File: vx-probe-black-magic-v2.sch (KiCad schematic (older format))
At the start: 31 parts, among them P1 USB MINI B, U1 stm32f070-qfp48, U2 AT45DB321D-SU, Y1 8 MHz

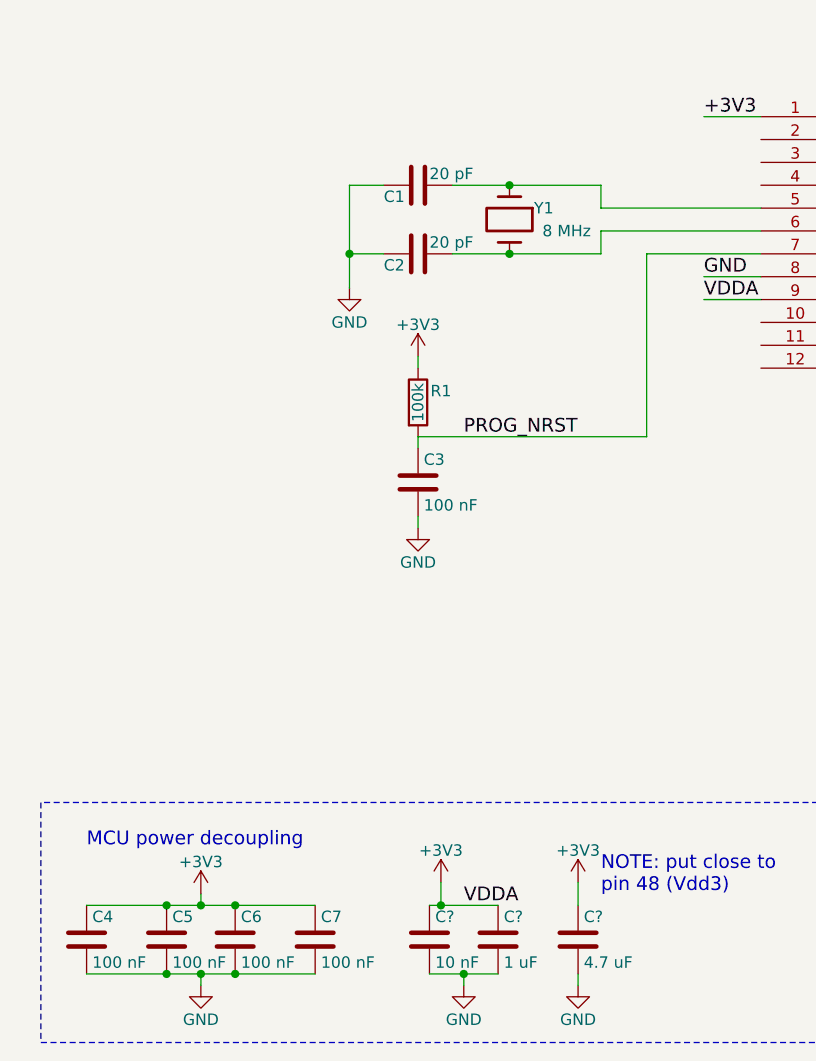
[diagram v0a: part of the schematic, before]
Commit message: made capacitor values more readable
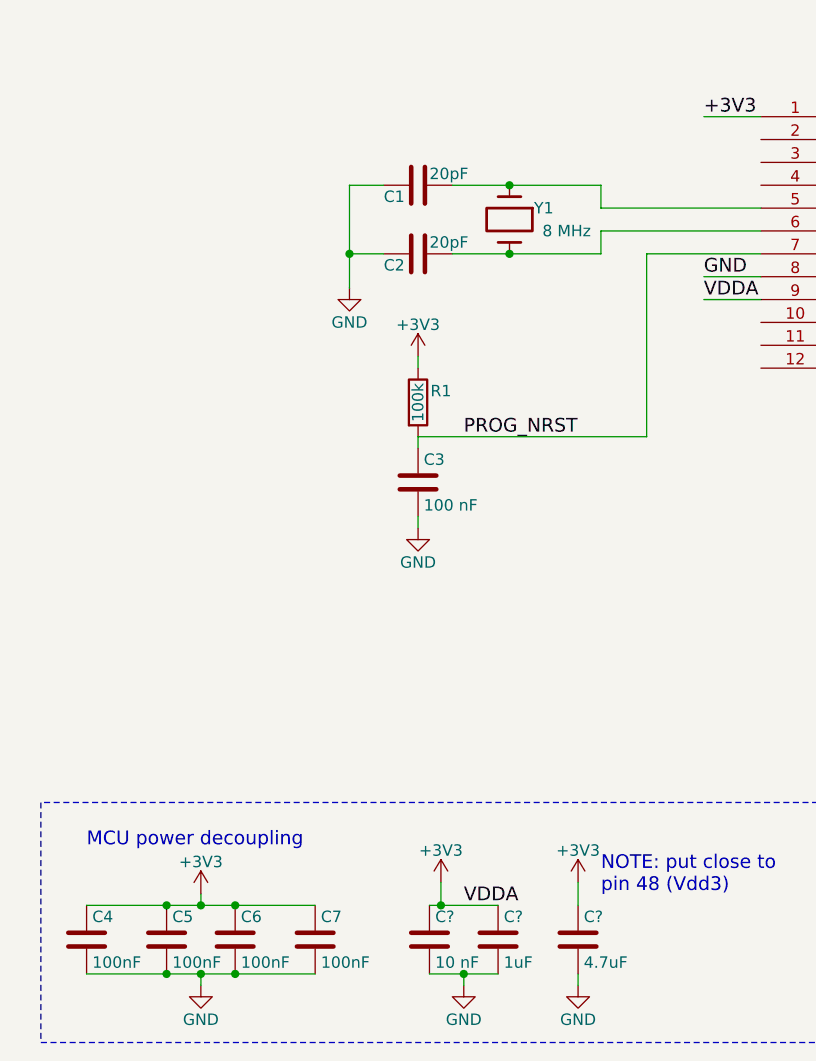
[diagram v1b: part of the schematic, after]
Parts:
- C1, C2: value 20 pF -> 20pF
- C4, C5, C6, C7: value 100 nF -> 100nF
- C?: value 1 uF -> 1uF
- C?: value 4.7 uF -> 4.7uF
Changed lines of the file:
@@
 P 2500 3750
 F 0 "C1" V 2550 3600 50  0000 L CNN
-F 1 "20 pF" V 2450 3800 50  0000 L CNN
+F 1 "20pF" V 2450 3800 50  0000 L CNN
 F 2 "Capacitors_SMD:C_0805" H 2538 3600 50  0001 C CNN
 F 3 "" H 2500 3750 50  0000 C CNN
@@
 P 2500 4050
 F 0 "C2" V 2550 3900 50  0000 L CNN
-F 1 "20 pF" V 2450 4100 50  0000 L CNN
+F 1 "20pF" V 2450 4100 50  0000 L CNN
 F 2 "Capacitors_SMD:C_0805" H 2538 3900 50  0001 C CNN
 F 3 "" H 2500 4050 50  0000 C CNN
@@
 P 1050 7050
 F 0 "C4" H 1075 7150 50  0000 L CNN
-F 1 "100 nF" H 1075 6950 50  0000 L CNN
+F 1 "100nF" H 1075 6950 50  0000 L CNN
 F 2 "Capacitors_SMD:C_0805" H 1088 6900 50  0001 C CNN
 F 3 "" H 1050 7050 50  0000 C CNN
@@
 P 1400 7050
 F 0 "C5" H 1425 7150 50  0000 L CNN
-F 1 "100 nF" H 1425 6950 50  0000 L CNN
+F 1 "100nF" H 1425 6950 50  0000 L CNN
 F 2 "Capacitors_SMD:C_0805" H 1438 6900 50  0001 C CNN
 F 3 "" H 1400 7050 50  0000 C CNN
@@
 P 1700 7050
 F 0 "C6" H 1725 7150 50  0000 L CNN
-F 1 "100 nF" H 1725 6950 50  0000 L CNN
+F 1 "100nF" H 1725 6950 50  0000 L CNN
 F 2 "Capacitors_SMD:C_0805" H 1738 6900 50  0001 C CNN
 F 3 "" H 1700 7050 50  0000 C CNN
@@
 P 2050 7050
 F 0 "C7" H 2075 7150 50  0000 L CNN
-F 1 "100 nF" H 2075 6950 50  0000 L CNN
+F 1 "100nF" H 2075 6950 50  0000 L CNN
 F 2 "Capacitors_SMD:C_0805" H 2088 6900 50  0001 C CNN
 F 3 "" H 2050 7050 50  0000 C CNN
@@
 P 2850 7050
 F 0 "C?" H 2875 7150 50  0000 L CNN
-F 1 "1 uF" H 2875 6950 50  0000 L CNN
+F 1 "1uF" H 2875 6950 50  0000 L CNN
 F 2 "" H 2888 6900 50  0000 C CNN
 F 3 "" H 2850 7050 50  0000 C CNN
@@
 P 3200 7050
 F 0 "C?" H 3225 7150 50  0000 L CNN
-F 1 "4.7 uF" H 3225 6950 50  0000 L CNN
+F 1 "4.7uF" H 3225 6950 50  0000 L CNN
 F 2 "" H 3238 6900 50  0000 C CNN
 F 3 "" H 3200 7050 50  0000 C CNN

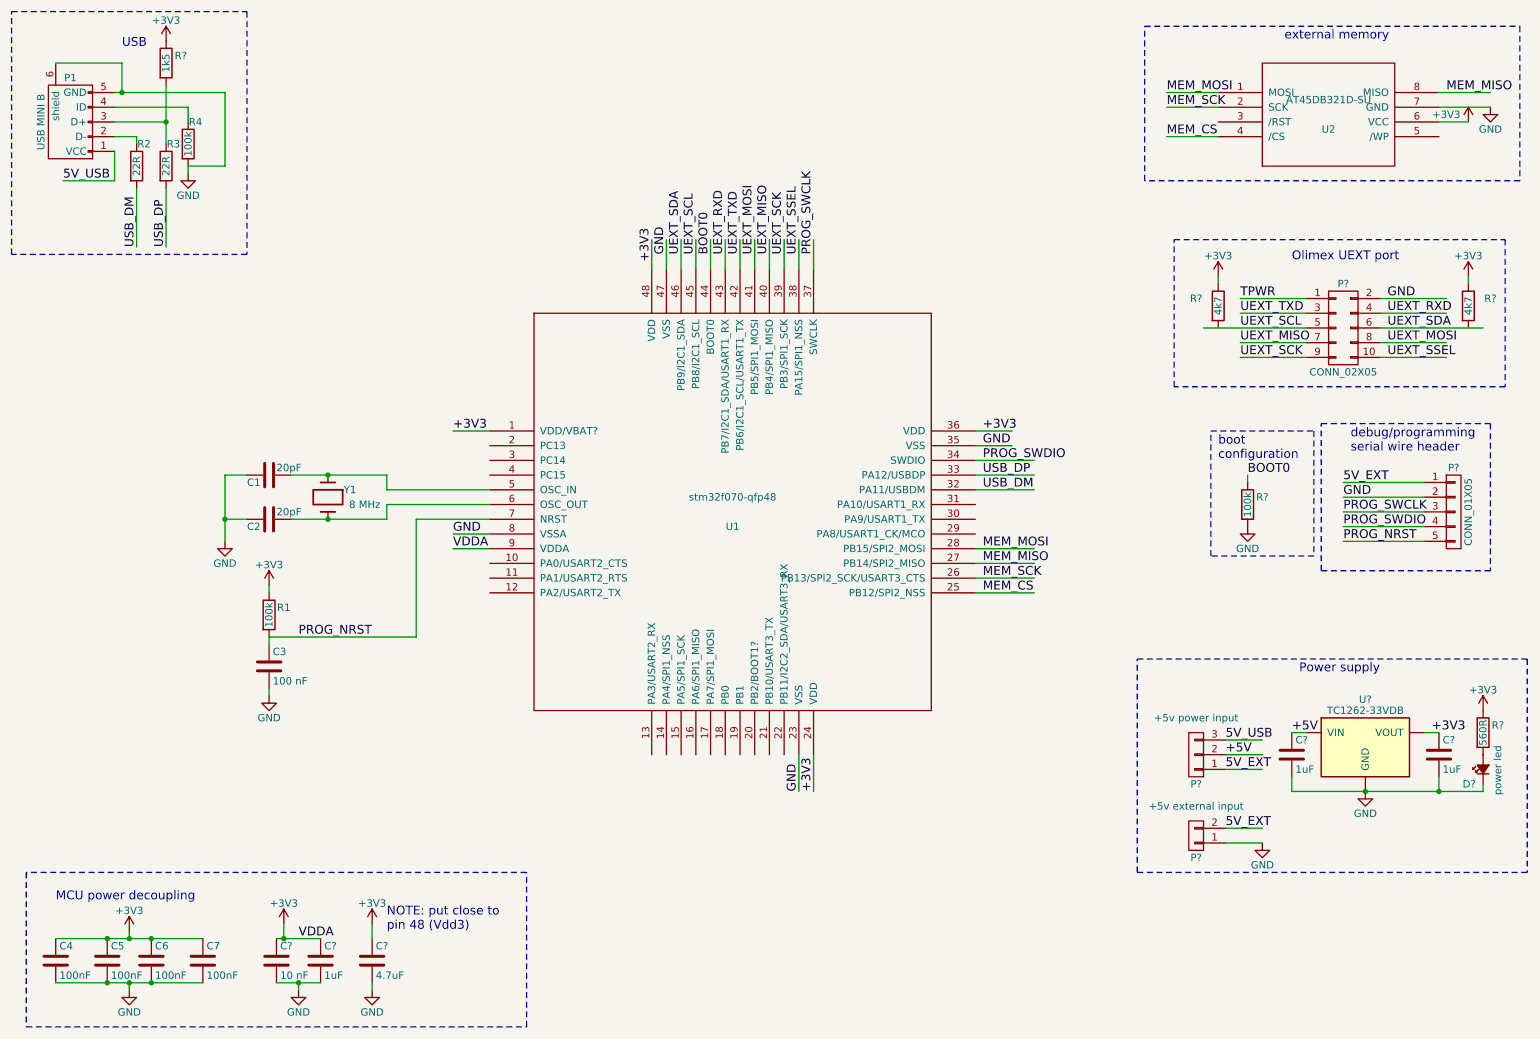
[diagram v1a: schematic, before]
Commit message: updated components' annotations and footprints
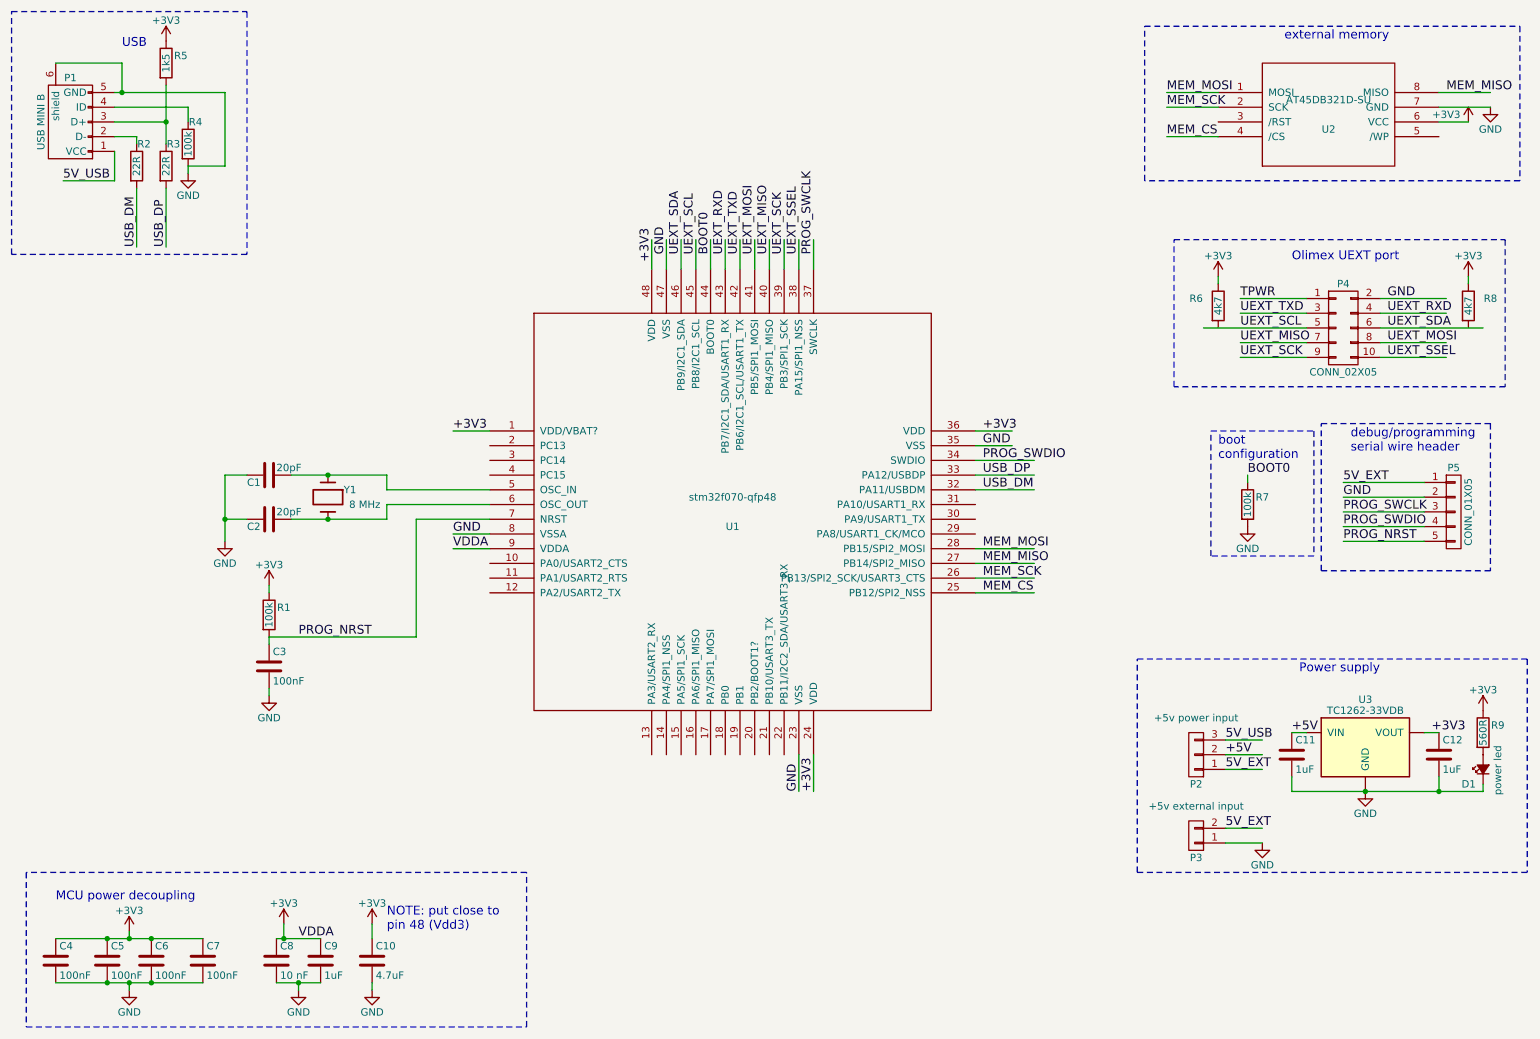
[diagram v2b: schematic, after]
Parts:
- C10, C11, C12, C8, C9: renamed from C?; footprint (none) -> Capacitors_SMD:C_0805
- C3: value 100 nF -> 100nF
- D1: renamed from D?; footprint (none) -> LEDs:LED_0805
- P2: renamed from P?; footprint (none) -> Pin_Headers:Pin_Header_Straight_1x03
- P3: renamed from P?; footprint (none) -> Pin_Headers:Pin_Header_Straight_1x02
- P4: renamed from P?; footprint (none) -> Pin_Headers:Pin_Header_Straight_2x05
- P5: renamed from P?; footprint (none) -> Pin_Headers:Pin_Header_Straight_1x05
- R5, R6, R7, R8, R9: renamed from R?; footprint (none) -> Resistors_SMD:R_0805
- U3: renamed from U?; footprint SOT-223 -> TO_SOT_Packages_SMD:SOT-223
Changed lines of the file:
@@
 P 2500 5050
 F 0 "C3" H 2525 5150 50  0000 L CNN
-F 1 "100 nF" H 2525 4950 50  0000 L CNN
+F 1 "100nF" H 2525 4950 50  0000 L CNN
 F 2 "Capacitors_SMD:C_0805" H 2538 4900 50  0001 C CNN
 F 3 "" H 2500 5050 50  0000 C CNN
@@
 MEM_MISO
 $Comp
-L +3V3 #PWR?
+L +3V3 #PWR07
 U 1 1 57D8566A
 P 10650 1350
-F 0 "#PWR?" H 10650 1200 50  0001 C CNN
+F 0 "#PWR07" H 10650 1200 50  0001 C CNN
 F 1 "+3V3" H 10500 1400 50  0000 C CNN
 F 2 "" H 10650 1350 50  0000 C CNN
@@
 $EndComp
 $Comp
-L GND #PWR?
+L GND #PWR08
 U 1 1 57D856D3
 P 10800 1250
-F 0 "#PWR?" H 10800 1000 50  0001 C CNN
+F 0 "#PWR08" H 10800 1000 50  0001 C CNN
 F 1 "GND" H 10800 1100 50  0000 C CNN
 F 2 "" H 10800 1250 50  0000 C CNN
@@
 external memory
 $Comp
-L CONN_02X05 P?
+L CONN_02X05 P4
 U 1 1 57D86033
 P 9800 2750
-F 0 "P?" H 9800 3050 50  0000 C CNN
+F 0 "P4" H 9800 3050 50  0000 C CNN
 F 1 "CONN_02X05" H 9800 2450 50  0000 C CNN
-F 2 "" H 9800 1550 50  0000 C CNN
+F 2 "Pin_Headers:Pin_Header_Straight_2x05" H 9800 1550 50  0001 C CNN
 F 3 "" H 9800 1550 50  0000 C CNN
 	1    9800 2750
@@
 UEXT_SSEL
 $Comp
-L R R?
+L R R6
 U 1 1 57D8663E
 P 8950 2600
-F 0 "R?" H 8800 2650 50  0000 C CNN
+F 0 "R6" H 8800 2650 50  0000 C CNN
 F 1 "4k7" V 8950 2600 50  0000 C CNN
-F 2 "" V 8880 2600 50  0000 C CNN
+F 2 "Resistors_SMD:R_0805" V 8880 2600 50  0001 C CNN
 F 3 "" H 8950 2600 50  0000 C CNN
 	1    8950 2600
@@
 $EndComp
 $Comp
-L +3V3 #PWR?
+L +3V3 #PWR09
 U 1 1 57D86D6F
 P 8950 2400
-F 0 "#PWR?" H 8950 2250 50  0001 C CNN
+F 0 "#PWR09" H 8950 2250 50  0001 C CNN
 F 1 "+3V3" H 8950 2540 50  0000 C CNN
 F 2 "" H 8950 2400 50  0000 C CNN
@@
 $EndComp
 $Comp
-L R R?
+L R R8
 U 1 1 57D86DD6
 P 10650 2600
-F 0 "R?" H 10800 2650 50  0000 C CNN
+F 0 "R8" H 10800 2650 50  0000 C CNN
 F 1 "4k7" V 10650 2600 50  0000 C CNN
-F 2 "" V 10580 2600 50  0000 C CNN
+F 2 "Resistors_SMD:R_0805" V 10580 2600 50  0001 C CNN
 F 3 "" H 10650 2600 50  0000 C CNN
 	1    10650 2600
@@
 $EndComp
 $Comp
-L +3V3 #PWR?
+L +3V3 #PWR010
 U 1 1 57D86DDD
 P 10650 2400
-F 0 "#PWR?" H 10650 2250 50  0001 C CNN
+F 0 "#PWR010" H 10650 2250 50  0001 C CNN
 F 1 "+3V3" H 10650 2540 50  0000 C CNN
 F 2 "" H 10650 2400 50  0000 C CNN
@@
 VDDA
 $Comp
-L C C?
+L C C8
 U 1 1 57D889A2
 P 2550 7050
-F 0 "C?" H 2575 7150 50  0000 L CNN
+F 0 "C8" H 2575 7150 50  0000 L CNN
 F 1 "10 nF" H 2575 6950 50  0000 L CNN
-F 2 "" H 2588 6900 50  0000 C CNN
+F 2 "Capacitors_SMD:C_0805" H 2588 6900 50  0001 C CNN
 F 3 "" H 2550 7050 50  0000 C CNN
 	1    2550 7050
@@
 $EndComp
 $Comp
-L C C?
+L C C9
 U 1 1 57D88A0C
 P 2850 7050
-F 0 "C?" H 2875 7150 50  0000 L CNN
+F 0 "C9" H 2875 7150 50  0000 L CNN
 F 1 "1uF" H 2875 6950 50  0000 L CNN
-F 2 "" H 2888 6900 50  0000 C CNN
+F 2 "Capacitors_SMD:C_0805" H 2888 6900 50  0001 C CNN
 F 3 "" H 2850 7050 50  0000 C CNN
 	1    2850 7050
@@
 $EndComp
 $Comp
-L GND #PWR?
+L GND #PWR011
 U 1 1 57D88BF4
 P 2700 7250
-F 0 "#PWR?" H 2700 7000 50  0001 C CNN
+F 0 "#PWR011" H 2700 7000 50  0001 C CNN
 F 1 "GND" H 2700 7100 50  0000 C CNN
 F 2 "" H 2700 7250 50  0000 C CNN
@@
 $EndComp
 $Comp
-L +3V3 #PWR?
+L +3V3 #PWR012
 U 1 1 57D88CB2
 P 2600 6800
-F 0 "#PWR?" H 2600 6650 50  0001 C CNN
+F 0 "#PWR012" H 2600 6650 50  0001 C CNN
 F 1 "+3V3" H 2600 6940 50  0000 C CNN
 F 2 "" H 2600 6800 50  0000 C CNN
@@
 VDDA
 $Comp
-L C C?
+L C C10
 U 1 1 57D88F0B
 P 3200 7050
-F 0 "C?" H 3225 7150 50  0000 L CNN
+F 0 "C10" H 3225 7150 50  0000 L CNN
 F 1 "4.7uF" H 3225 6950 50  0000 L CNN
-F 2 "" H 3238 6900 50  0000 C CNN
+F 2 "Capacitors_SMD:C_0805" H 3238 6900 50  0001 C CNN
 F 3 "" H 3200 7050 50  0000 C CNN
 	1    3200 7050
@@
 $EndComp
 $Comp
-L GND #PWR?
+L GND #PWR013
 U 1 1 57D88FD9
 P 3200 7250
-F 0 "#PWR?" H 3200 7000 50  0001 C CNN
+F 0 "#PWR013" H 3200 7000 50  0001 C CNN
 F 1 "GND" H 3200 7100 50  0000 C CNN
 F 2 "" H 3200 7250 50  0000 C CNN
@@
 $EndComp
 $Comp
-L +3V3 #PWR?
+L +3V3 #PWR014
 U 1 1 57D890F4
 P 3200 6800
-F 0 "#PWR?" H 3200 6650 50  0001 C CNN
+F 0 "#PWR014" H 3200 6650 50  0001 C CNN
 F 1 "+3V3" H 3200 6940 50  0000 C CNN
 F 2 "" H 3200 6800 50  0000 C CNN
@@
 NOTE: put close to\npin 48 (Vdd3)
 $Comp
-L R R?
+L R R5
 U 1 1 57D89DD6
 P 1800 950
-F 0 "R?" H 1900 1000 50  0000 C CNN
+F 0 "R5" H 1900 1000 50  0000 C CNN
 F 1 "1k5" V 1800 950 50  0000 C CNN
-F 2 "" V 1730 950 50  0000 C CNN
+F 2 "Resistors_SMD:R_0805" V 1730 950 50  0001 C CNN
 F 3 "" H 1800 950 50  0000 C CNN
 	1    1800 950
@@
 $EndComp
 $Comp
-L +3V3 #PWR?
+L +3V3 #PWR015
 U 1 1 57D89E25
 P 1800 800
-F 0 "#PWR?" H 1800 650 50  0001 C CNN
+F 0 "#PWR015" H 1800 650 50  0001 C CNN
 F 1 "+3V3" H 1800 940 50  0000 C CNN
 F 2 "" H 1800 800 50  0000 C CNN
@@
 PROG_SWCLK
 $Comp
-L CONN_01X05 P?
+L CONN_01X05 P5
 U 1 1 57D8BC7C
 P 10550 4000
-F 0 "P?" H 10550 4300 50  0000 C CNN
+F 0 "P5" H 10550 4300 50  0000 C CNN
 F 1 "CONN_01X05" V 10650 4000 50  0000 C CNN
-F 2 "" H 10550 4000 50  0000 C CNN
+F 2 "Pin_Headers:Pin_Header_Straight_1x05" H 10550 4000 50  0001 C CNN
 F 3 "" H 10550 4000 50  0000 C CNN
 	1    10550 4000
@@
 boot\nconfiguration
 $Comp
-L R R?
+L R R7
 U 1 1 57D8D839
 P 9150 3950
-F 0 "R?" H 9250 4000 50  0000 C CNN
+F 0 "R7" H 9250 4000 50  0000 C CNN
 F 1 "100k" V 9150 3950 50  0000 C CNN
-F 2 "" V 9080 3950 50  0000 C CNN
+F 2 "Resistors_SMD:R_0805" V 9080 3950 50  0001 C CNN
 F 3 "" H 9150 3950 50  0000 C CNN
 	1    9150 3950
@@
 $EndComp
 $Comp
-L GND #PWR?
+L GND #PWR016
 U 1 1 57D8DA47
 P 9150 4100
-F 0 "#PWR?" H 9150 3850 50  0001 C CNN
+F 0 "#PWR016" H 9150 3850 50  0001 C CNN
 F 1 "GND" H 9150 3950 50  0000 C CNN
 F 2 "" H 9150 4100 50  0000 C CNN
@@
 BOOT0
 $Comp
-L TC1262-33VDB U?
+L TC1262-33VDB U3
 U 1 1 57D8E183
 P 9950 5600
-F 0 "U?" H 9950 5925 50  0000 C CNN
+F 0 "U3" H 9950 5925 50  0000 C CNN
 F 1 "TC1262-33VDB" H 9950 5850 50  0000 C CNN
-F 2 "SOT-223" H 10000 5350 50  0001 L CIN
+F 2 "TO_SOT_Packages_SMD:SOT-223" H 10000 5350 50  0001 L CIN
 F 3 "" H 9950 5400 50  0001 C CNN
 	1    9950 5600
@@
 $EndComp
 $Comp
-L C C?
+L C C12
 U 1 1 57D8E350
 P 10450 5650
-F 0 "C?" H 10475 5750 50  0000 L CNN
+F 0 "C12" H 10475 5750 50  0000 L CNN
 F 1 "1uF" H 10475 5550 50  0000 L CNN
-F 2 "" H 10488 5500 50  0000 C CNN
+F 2 "Capacitors_SMD:C_0805" H 10488 5500 50  0001 C CNN
 F 3 "" H 10450 5650 50  0000 C CNN
 	1    10450 5650
@@
 $EndComp
 $Comp
-L C C?
+L C C11
 U 1 1 57D8E408
 P 9450 5650
-F 0 "C?" H 9475 5750 50  0000 L CNN
+F 0 "C11" H 9475 5750 50  0000 L CNN
 F 1 "1uF" H 9475 5550 50  0000 L CNN
-F 2 "" H 9488 5500 50  0000 C CNN
+F 2 "Capacitors_SMD:C_0805" H 9488 5500 50  0001 C CNN
 F 3 "" H 9450 5650 50  0000 C CNN
 	1    9450 5650
@@
 +5V
 $Comp
-L GND #PWR?
+L GND #PWR017
 U 1 1 57D8EA04
 P 9950 5900
-F 0 "#PWR?" H 9950 5650 50  0001 C CNN
+F 0 "#PWR017" H 9950 5650 50  0001 C CNN
 F 1 "GND" H 9950 5750 50  0000 C CNN
 F 2 "" H 9950 5900 50  0000 C CNN
@@
 $EndComp
 $Comp
-L R R?
+L R R9
 U 1 1 57D8EC19
 P 10750 5500
-F 0 "R?" H 10850 5550 50  0000 C CNN
+F 0 "R9" H 10850 5550 50  0000 C CNN
 F 1 "560R" V 10750 5500 50  0000 C CNN
-F 2 "" V 10680 5500 50  0000 C CNN
+F 2 "Resistors_SMD:R_0805" V 10680 5500 50  0001 C CNN
 F 3 "" H 10750 5500 50  0000 C CNN
 	1    10750 5500
@@
 $EndComp
 $Comp
-L Led_Small D?
+L Led_Small D1
 U 1 1 57D8EDD4
 P 10750 5750
-F 0 "D?" V 10650 5800 50  0000 L CNN
+F 0 "D1" V 10650 5800 50  0000 L CNN
 F 1 "power led" H 10575 5650 50  0000 L CNN
-F 2 "" V 10750 5750 50  0000 C CNN
+F 2 "LEDs:LED_0805" V 10750 5750 50  0001 C CNN
 F 3 "" V 10750 5750 50  0000 C CNN
 	1    10750 5750
@@
 Connection ~ 10450 5900
 $Comp
-L +3V3 #PWR?
+L +3V3 #PWR018
 U 1 1 57D8F462
 P 10750 5350
-F 0 "#PWR?" H 10750 5200 50  0001 C CNN
+F 0 "#PWR018" H 10750 5200 50  0001 C CNN
 F 1 "+3V3" H 10750 5490 50  0000 C CNN
 F 2 "" H 10750 5350 50  0000 C CNN
@@
 $EndComp
 $Comp
-L CONN_01X03 P?
+L CONN_01X03 P2
 U 1 1 57D8FCD5
 P 8800 5650
-F 0 "P?" H 8800 5850 50  0000 C CNN
+F 0 "P2" H 8800 5850 50  0000 C CNN
 F 1 "+5v power input" H 8800 5400 50  0000 C CNN
-F 2 "" H 8800 5650 50  0000 C CNN
+F 2 "Pin_Headers:Pin_Header_Straight_1x03" H 8800 5650 50  0001 C CNN
 F 3 "" H 8800 5650 50  0000 C CNN
 	1    8800 5650
@@
 5V_EXT
 $Comp
-L CONN_01X02 P?
+L CONN_01X02 P3
 U 1 1 57D91002
 P 8800 6200
-F 0 "P?" H 8800 6350 50  0000 C CNN
+F 0 "P3" H 8800 6350 50  0000 C CNN
 F 1 "+5v external input" H 8800 6000 50  0000 C CNN
-F 2 "" H 8800 6200 50  0000 C CNN
+F 2 "Pin_Headers:Pin_Header_Straight_1x02" H 8800 6200 50  0001 C CNN
 F 3 "" H 8800 6200 50  0000 C CNN
 	1    8800 6200
@@
 	9000 6250 9250 6250
 $Comp
-L GND #PWR?
+L GND #PWR019
 U 1 1 57D912A1
 P 9250 6250
-F 0 "#PWR?" H 9250 6000 50  0001 C CNN
+F 0 "#PWR019" H 9250 6000 50  0001 C CNN
 F 1 "GND" H 9250 6100 50  0000 C CNN
 F 2 "" H 9250 6250 50  0000 C CNN
